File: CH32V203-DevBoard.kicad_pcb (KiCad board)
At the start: 2 copper layers, 20.3 x 50.8 mm, 41 parts, among them J1 USB_C_Receptacle_USB2.0_16P, J2 USB_C_Receptacle_USB2.0_16P, SW1 SW_Push, SW2 SW_Push, SW3 SW_Push, U1 CH32V203C8T6, U2 RT9080-33GJ5

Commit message: cc resistor fix
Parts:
- R6, R7: value 51kΩ -> 47kΩ
- R8, R9: value 12kΩ -> 10kΩ

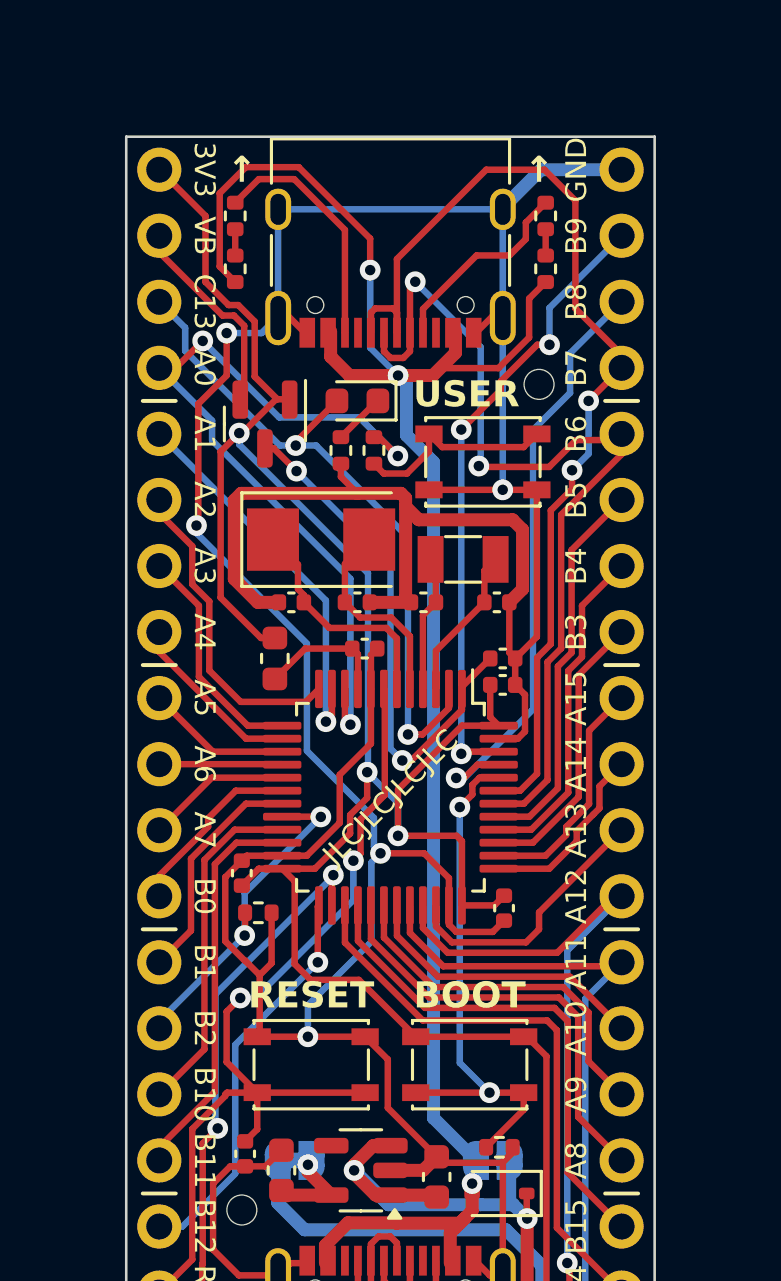
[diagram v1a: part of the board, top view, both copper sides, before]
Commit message: add host vbus switch
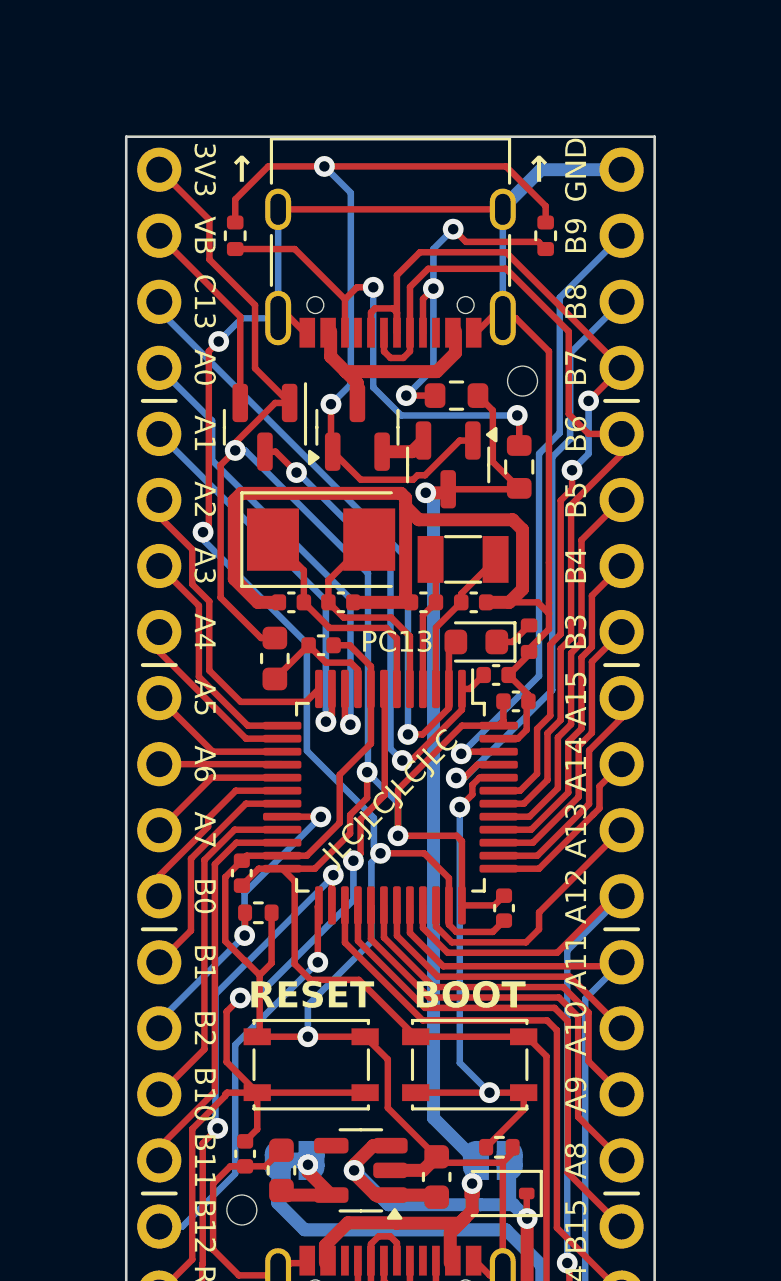
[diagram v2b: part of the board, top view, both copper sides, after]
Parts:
- removed R10: 330Ω, Resistor_SMD:R_0402_1005Metric
- removed SW3: SW_Push, Button_Switch_SMD:SW_SPST_PTS810
- added Q1: AO3401A, Package_TO_SOT_SMD:SOT-23, F.Cu at (139.4, 88.8)
- added Q2: AO3401A, Package_TO_SOT_SMD:SOT-23, F.Cu at (135.9, 87.4)
- R6, R7: value 47kΩ -> 56kΩ; footprint Resistor_SMD:R_0402_1005Metric -> Resistor_SMD:R_0603_1608Metric
- R8, R9: value 10kΩ -> 1MΩ
- moved R7 13.3 mm to (142.1, 88.9), turned to -90 degrees
- moved LED1 10.3 mm to (140.5, 95.6)
- moved R3 10.2 mm to (142.5, 95.5)
- moved R6 5.96 mm to (139.7, 86.2), turned to 0 degrees
- moved C10 1.68 mm to (134.5, 95.8)
- moved C1 0.89 mm to (140.4, 94.1)
- moved C9 0.81 mm to (142.0, 97.9)
- moved R8 0.76 mm to (143.1, 80.0), turned to -90 degrees
- moved R9 0.76 mm to (131.2, 80.0)
- moved C5 0.68 mm to (141.2, 96.9)
- moved H2 0.65 mm to (142.2, 85.6)
- moved C3 0.63 mm to (135.3, 94.1)
- moved D2 0.13 mm to (132.3, 87.4)
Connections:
- J2 pad A4: VBUS -> Net-(Q2-D)
- J2 pad A9: VBUS -> Net-(Q2-D)
- J2 pad B4: VBUS -> Net-(Q2-D)
- J2 pad B9: VBUS -> Net-(Q2-D)
- R6 pad 1: VBUS -> Net-(J2-CC1)
- R6 pad 2: Net-(R6-Pad2) -> VBUS
- R7 pad 1: VBUS -> Net-(J2-CC2)
- R7 pad 2: Net-(R7-Pad2) -> VBUS
- R8 pad 1: Net-(R6-Pad2) -> Net-(Q1-G)
- R9 pad 1: Net-(R7-Pad2) -> Net-(J2-CC2)
- R9 pad 2: Net-(J2-CC2) -> Net-(Q1-G)
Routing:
- net Net-(Q1-G): track 0.00 -> 32.9 mm, vias 0 -> 2
- net VBUS: track 73.0 -> 45.6 mm, vias 3 -> 2
- net PA0: track 30.9 -> 18.2 mm, vias 3 -> 1
- net Net-(J2-CC2): track 9.36 -> 18.6 mm, vias 0 -> 2
- net Net-(Q2-D): track 0.00 -> 8.54 mm
- net Net-(R10-Pad2): track 7.87 -> 0.00 mm
- net Net-(J2-CC1): track 7.70 -> 14.0 mm, vias 0 -> 3
- net PB7: track 40.2 -> 34.4 mm
- net GND: track 197.1 -> 194.6 mm, vias 5 -> 4
- net Net-(Q1-S): track 0.00 -> 1.77 mm
- net PB6: track 35.6 -> 34.1 mm, vias 2 -> 0
- net PC13: track 26.5 -> 25.2 mm, vias 2 -> 1
- net +3V3: track 107.9 -> 106.8 mm
- net Net-(R7-Pad2): track 1.01 -> 0.00 mm
- net Net-(R6-Pad2): track 1.01 -> 0.00 mm
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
